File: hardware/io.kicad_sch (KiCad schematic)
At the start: 29 parts, among them Q1 DMP10H400SE, Q2 BSS123, U10 STS4X, U11 LTR-329ALS-01, U3 MCP2542FDxMF, U9 74LVC1G17

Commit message: 📂 PCB updates
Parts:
- C11: footprint (none) -> Capacitor_SMD:C_0805_2012Metric
- C13: footprint (none) -> Capacitor_SMD:C_0603_1608Metric
- R14, R15, R16: footprint PCM_Resistor_SMD_AKL:R_0603_1608Metric -> Resistor_SMD:R_0603_1608Metric
- R17, R18, R19, R20, R7: footprint (none) -> Resistor_SMD:R_0603_1608Metric
- R5, R6: footprint (none) -> Resistor_SMD:R_0805_2012Metric
- U11: footprint LTR-329ALS-01_LTO -> PEAK:LTR-329ALS-01_LTO
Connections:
- net VBUS: no longer DZ1.3 (K), Q1.3 (S), R5.1
- new net +BATT: DZ1.3 (K), Q1.3 (S), R5.1
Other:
- moved on the sheet: C11
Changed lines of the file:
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@@
 	(wire
 		(pts
-			(xy 127 46.99) (xy 127 66.04)
+			(xy 127 49.53) (xy 127 66.04)
 		)
 		(stroke
@@
 	(wire
 		(pts
+			(xy 127 41.91) (xy 127 39.37)
+		)
+		(stroke
+			(width 0)
+			(type default)
+		)
+	)
+	(wire
+		(pts
 			(xy 101.6 55.88) (xy 102.87 55.88)
 		)
@@
 			)
 		)
-		(property "Footprint" ""
+		(property "Footprint" "Resistor_SMD:R_0603_1608Metric"
 			(at 98.552 90.17 90)
 			(effects
@@
 			)
 		)
-		(property "Footprint" "PCM_Resistor_SMD_AKL:R_0603_1608Metric"
+		(property "Footprint" "Resistor_SMD:R_0603_1608Metric"
 			(at 62.992 30.48 90)
 			(effects
@@
 			)
 		)
-		(property "Footprint" ""
+		(property "Footprint" "Resistor_SMD:R_0805_2012Metric"
 			(at 118.872 45.72 90)
 			(effects
@@
 			)
 		)
-		(property "Footprint" "LTR-329ALS-01_LTO"
+		(property "Footprint" "PEAK:LTR-329ALS-01_LTO"
 			(at 218.44 59.69 0)
 			(effects
@@
 			)
 		)
-		(property "Footprint" ""
+		(property "Footprint" "Capacitor_SMD:C_0603_1608Metric"
 			(at 94.9452 105.41 0)
 			(effects
@@
 	)
 	(symbol
-		(lib_id "power:VBUS")
-		(at 135.89 26.67 0)
-		(unit 1)
-		(exclude_from_sim no)
-		(in_bom yes)
-		(on_board yes)
-		(dnp no)
-		(fields_autoplaced yes)
-		(property "Reference" "#PWR029"
-			(at 135.89 30.48 0)
-			(effects
-				(font
-					(size 1.27 1.27)
-				)
-				(hide yes)
-			)
-		)
-		(property "Value" "VBUS"
-			(at 135.89 21.59 0)
-			(effects
-				(font
-					(size 1.27 1.27)
-				)
-			)
-		)
-		(property "Footprint" ""
-			(at 135.89 26.67 0)
-			(effects
-				(font
-					(size 1.27 1.27)
-				)
-				(hide yes)
-			)
-		)
-		(property "Datasheet" ""
-			(at 135.89 26.67 0)
-			(effects
-				(font
-					(size 1.27 1.27)
-				)
-				(hide yes)
-			)
-		)
-		(property "Description" "Power symbol creates a global label with name \"VBUS\""
-			(at 135.89 26.67 0)
-			(effects
-				(font
-					(size 1.27 1.27)
-				)
-				(hide yes)
-			)
-		)
-		(pin "1"
-		)
-		(instances
-			(project "peak"
-				(path "/54a54a18-4a65-4728-b17a-32b4a97370c1/0c93e6bb-f116-4211-a7bb-466a518707dd"
-					(reference "#PWR029")
-					(unit 1)
-				)
-			)
-			(project ""
-				(path "/bd2db347-40f3-4f25-9f46-975f5972e5df"
-					(reference "#PWR01")
-					(unit 1)
-				)
-			)
-		)
-	)
-	(symbol
 		(lib_id "Device:C")
 		(at 213.36 31.75 0)
@@
 			)
 		)
-		(property "Footprint" ""
+		(property "Footprint" "Resistor_SMD:R_0805_2012Metric"
 			(at 125.222 33.02 90)
 			(effects
@@
 	(symbol
 		(lib_id "Device:C")
-		(at 127 43.18 0)
+		(at 127 45.72 0)
 		(unit 1)
 		(exclude_from_sim no)
@@
 		(dnp no)
 		(property "Reference" "C11"
-			(at 127.254 45.212 0)
+			(at 127.254 47.752 0)
 			(effects
 				(font
@@
 		)
 		(property "Value" "100nF/100V"
-			(at 127.508 45.72 0)
+			(at 127.508 48.26 0)
 			(effects
 				(font
@@
 			)
 		)
-		(property "Footprint" ""
-			(at 127.9652 46.99 0)
+		(property "Footprint" "Capacitor_SMD:C_0805_2012Metric"
+			(at 127.9652 49.53 0)
 			(effects
 				(font
@@
 		)
 		(property "Datasheet" "~"
-			(at 127 43.18 0)
+			(at 127 45.72 0)
 			(effects
 				(font
@@
 		)
 		(property "Description" "Unpolarized capacitor"
-			(at 127 43.18 0)
+			(at 127 45.72 0)
 			(effects
 				(font
@@
 			)
 		)
-		(property "Footprint" "PCM_Resistor_SMD_AKL:R_0603_1608Metric"
+		(property "Footprint" "Resistor_SMD:R_0603_1608Metric"
 			(at 42.672 30.48 90)
 			(effects
@@
 	)
 	(symbol
+		(lib_id "power:+BATT")
+		(at 135.89 26.67 0)
+		(unit 1)
+		(exclude_from_sim no)
+		(in_bom yes)
+		(on_board yes)
+		(dnp no)
+		(fields_autoplaced yes)
+		(property "Reference" "#PWR044"
+			(at 135.89 30.48 0)
+			(effects
+				(font
+					(size 1.27 1.27)
+				)
+				(hide yes)
+			)
+		)
+		(property "Value" "+BATT"
+			(at 135.89 21.59 0)
+			(effects
+				(font
+					(size 1.27 1.27)
+				)
+			)
+		)
+		(property "Footprint" ""
+			(at 135.89 26.67 0)
+			(effects
+				(font
+					(size 1.27 1.27)
+				)
+				(hide yes)
+			)
+		)
+		(property "Datasheet" ""
+			(at 135.89 26.67 0)
+			(effects
+				(font
+					(size 1.27 1.27)
+				)
+				(hide yes)
+			)
+		)
+		(property "Description" "Power symbol creates a global label with name \"+BATT\""
+			(at 135.89 26.67 0)
+			(effects
+				(font
+					(size 1.27 1.27)
+				)
+				(hide yes)
+			)
+		)
+		(pin "1"
+		)
+		(instances
+			(project ""
+				(path "/54a54a18-4a65-4728-b17a-32b4a97370c1/0c93e6bb-f116-4211-a7bb-466a518707dd"
+					(reference "#PWR044")
+					(unit 1)
+				)
+			)
+		)
+	)
+	(symbol
 		(lib_id "power:GND")
 		(at 100.33 107.95 0)
@@
 			)
 		)
-		(property "Footprint" ""
+		(property "Footprint" "Resistor_SMD:R_0603_1608Metric"
 			(at 106.68 98.298 90)
 			(effects
@@
 			)
 		)
-		(property "Footprint" "PCM_Resistor_SMD_AKL:R_0603_1608Metric"
+		(property "Footprint" "Resistor_SMD:R_0603_1608Metric"
 			(at 21.082 30.48 90)
 			(effects
@@
 			)
 		)
-		(property "Footprint" ""
+		(property "Footprint" "Resistor_SMD:R_0603_1608Metric"
 			(at 109.982 60.96 90)
 			(effects
@@
 			)
 		)
-		(property "Footprint" ""
+		(property "Footprint" "Resistor_SMD:R_0603_1608Metric"
 			(at 106.68 57.658 90)
 			(effects
@@
 			)
 		)
-		(property "Footprint" ""
+		(property "Footprint" "Resistor_SMD:R_0603_1608Metric"
 			(at 98.552 101.6 90)
 			(effects

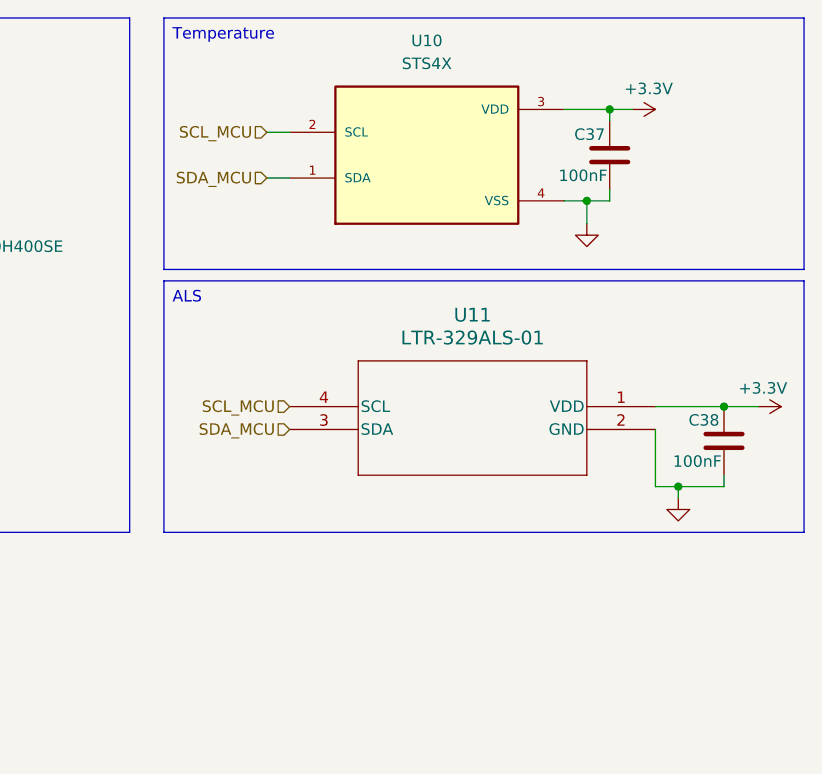
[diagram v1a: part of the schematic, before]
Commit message: 🐛 Fix errors from rev1.0
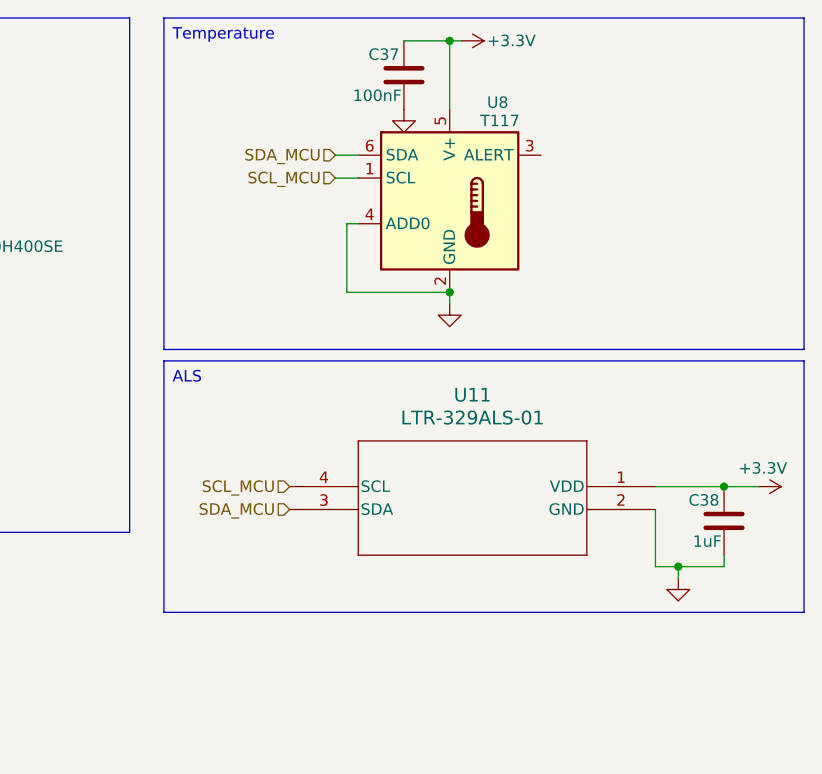
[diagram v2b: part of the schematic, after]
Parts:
- removed U10: STS4X, PEAK:STS4X, symbol STS4X:STS4X
- added U8: T117, PCM_Package_DFN_QFN_AKL:DFN-6-1EP_2x2mm_P0.65mm_EP1x1.6mm, symbol Sensor_Temperature:TMP117xxDRV
- C38: value 100nF -> 1uF
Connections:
- net +3.3V: now also U8.5 (V+)
- net GND: now also U8.2 (GND), U8.4 (ADD0)
- net SCL_MCU: now also U8.1 (SCL)
- net SDA_MCU: now also U8.6 (SDA)
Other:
- moved on the sheet: C37, C38, U11

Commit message: ✨ Final PCB updates
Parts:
- renumbered C34 to C601, C35 to C602, C36 to C603, C6 to C604, C5 to C605, C12 to C606, C11 to C607, C13 to C608, C37 to C609, C38 to C610, DZ1 to DZ601, Q2 to Q601, Q1 to Q602, R14 to R601, R15 to R602, R16 to R603, R3 to R604, R1 to R605, R7 to R606, R17 to R607, R6 to R608, R5 to R609, R18 to R610, R19 to R611, R20 to R612, U3 to U601, U9 to U602, U8 to U603, U11 to U604
